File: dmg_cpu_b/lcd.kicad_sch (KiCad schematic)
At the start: 119 parts

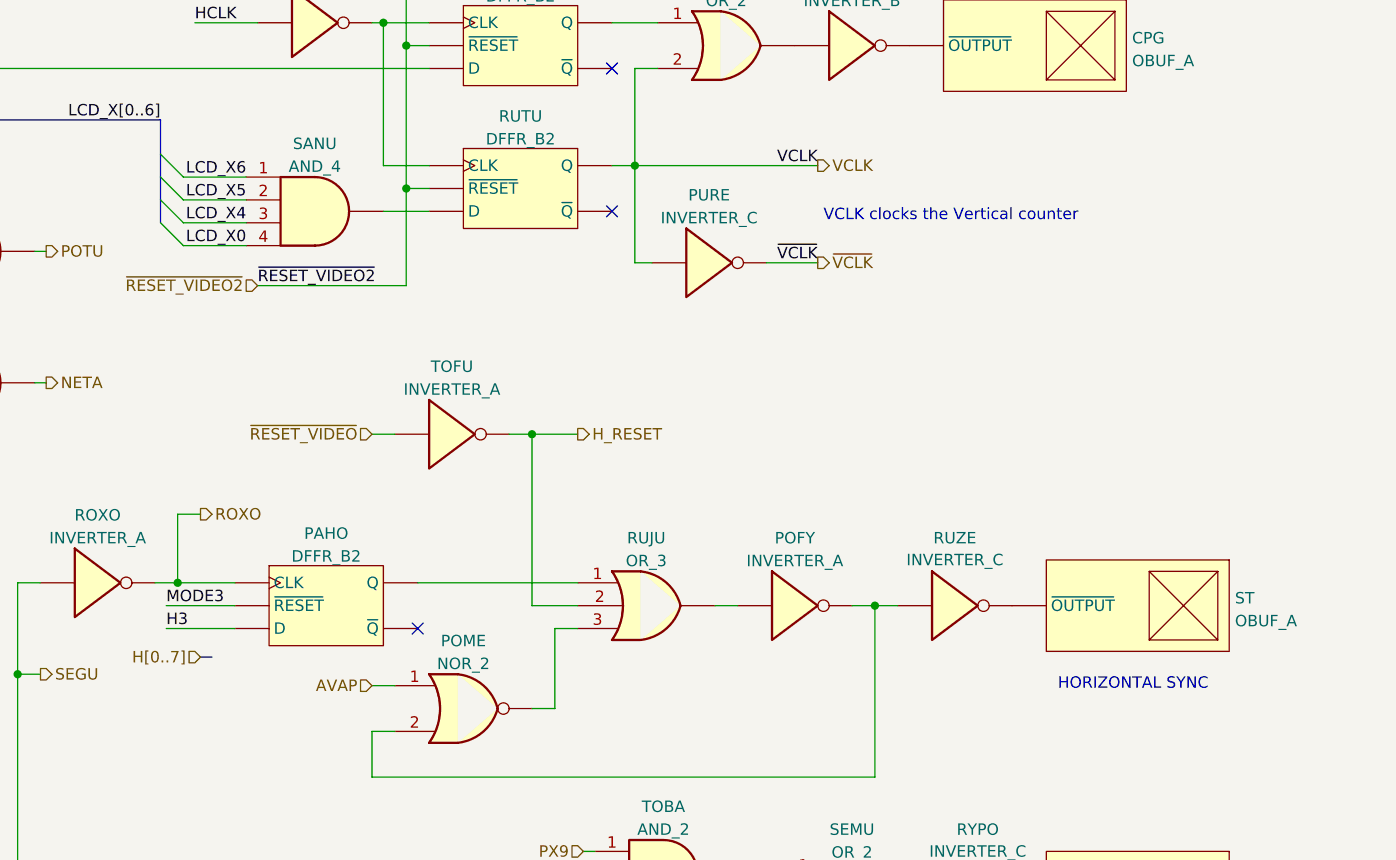
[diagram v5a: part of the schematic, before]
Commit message: more oam sheets added. Some are still work in progress.
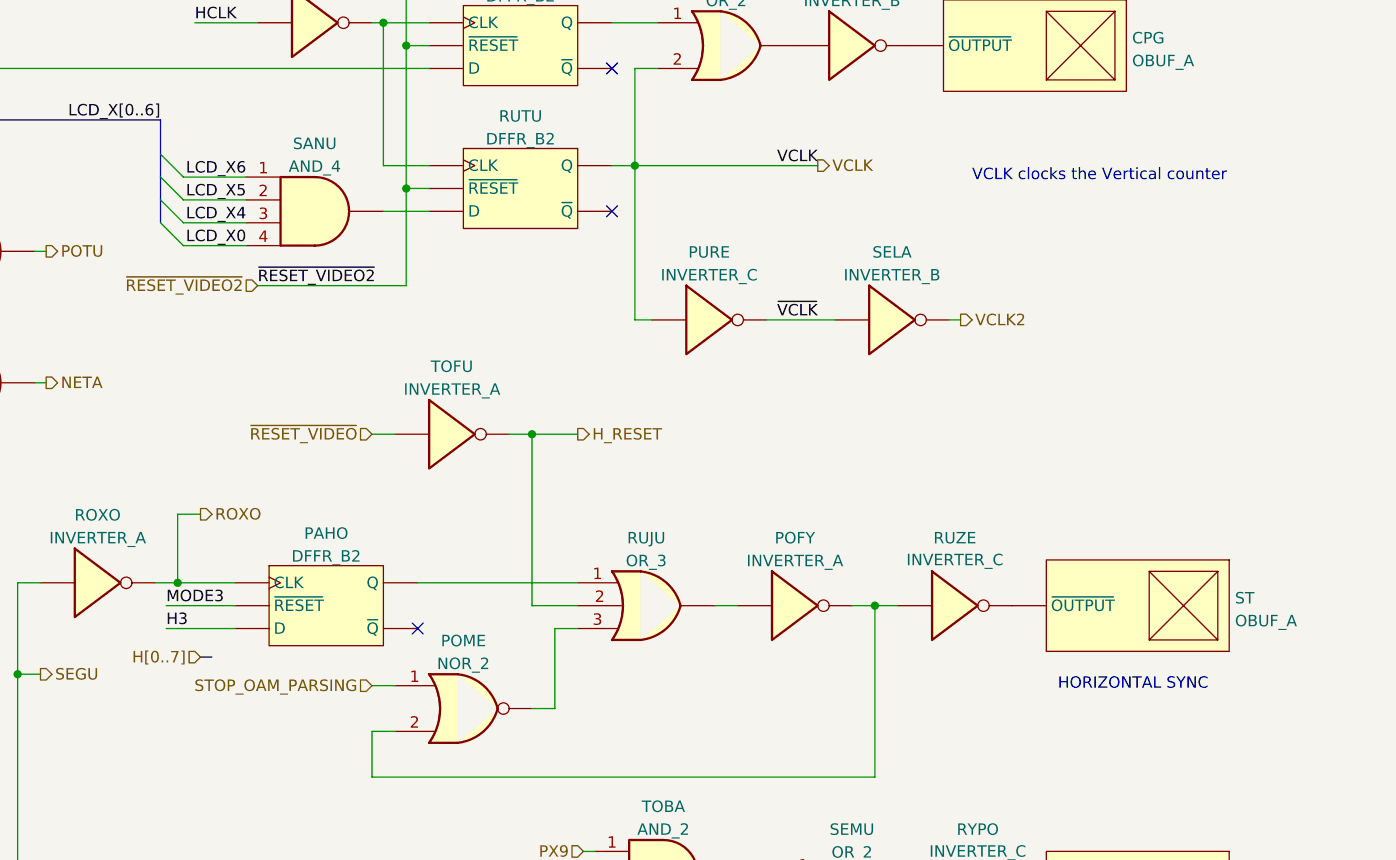
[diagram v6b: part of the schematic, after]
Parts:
- added SELA: INVERTER_B, symbol DMG_CPU_Cells:INVERTER_B
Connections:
- net ~{VCLK}: now also SELA.1
- net AVAP renamed STOP_OAM_PARSING
- new net VCLK2: SELA.2
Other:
- moved on the sheet: PURE
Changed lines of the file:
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@@
     (stroke (width 0) (type default) (color 0 0 0 0))
   )
-  (wire (pts (xy 327.025 173.99) (xy 325.12 173.99))
+  (wire (pts (xy 327.025 180.34) (xy 325.12 180.34))
     (stroke (width 0) (type default) (color 0 0 0 0))
   )
@@
     (stroke (width 0) (type default) (color 0 0 0 0))
   )
+  (wire (pts (xy 360.045 180.34) (xy 361.315 180.34))
+    (stroke (width 0) (type default) (color 0 0 0 0))
+  )
   (wire (pts (xy 322.58 163.195) (xy 325.12 163.195))
     (stroke (width 0) (type default) (color 0 0 0 0))
@@
     (stroke (width 0) (type default) (color 0 0 0 0))
   )
-  (wire (pts (xy 325.12 173.99) (xy 325.12 163.195))
+  (wire (pts (xy 325.12 180.34) (xy 325.12 163.195))
     (stroke (width 0) (type default) (color 0 0 0 0))
   )
@@
     (stroke (width 0) (type default) (color 0 0 0 0))
   )
-  (wire (pts (xy 339.725 173.99) (xy 345.44 173.99))
+  (wire (pts (xy 339.725 180.34) (xy 347.345 180.34))
     (stroke (width 0) (type default) (color 0 0 0 0))
   )
@@
     (effects (font (size 1.27 1.27)) (justify left bottom))
   )
-  (text "VCLK clocks the Vertical counter" (at 346.075 169.545 0)
+  (text "VCLK clocks the Vertical counter" (at 362.585 165.1 0)
     (effects (font (size 1.27 1.27)) (justify left bottom))
   )
@@
     (effects (font (size 1.27 1.27)) (justify left bottom))
   )
-  (label "~{VCLK}" (at 345.44 173.99 180)
+  (label "~{VCLK}" (at 345.44 180.34 180)
     (effects (font (size 1.27 1.27)) (justify right bottom))
   )
@@
     (effects (font (size 1.27 1.27)) (justify right))
   )
-  (hierarchical_label "AVAP" (shape input) (at 295.91 220.98 180)
+  (hierarchical_label "STOP_OAM_PARSING" (shape input) (at 295.91 220.98 180)
     (effects (font (size 1.27 1.27)) (justify right))
   )
@@
     (effects (font (size 1.27 1.27)) (justify left))
   )
+  (hierarchical_label "VCLK2" (shape output) (at 361.315 180.34 0)
+    (effects (font (size 1.27 1.27)) (justify left))
+  )
   (hierarchical_label "8192Hz" (shape input) (at 307.975 129.54 180)
     (effects (font (size 1.27 1.27)) (justify right))
   )
-  (hierarchical_label "~{VCLK}" (shape output) (at 345.44 173.99 0)
-    (effects (font (size 1.27 1.27)) (justify left))
-  )
   (hierarchical_label "FF40_D[0..7]" (shape input) (at 299.72 92.075 180)
     (effects (font (size 1.27 1.27)) (justify right))
@@
     (pin "2")
   )
-  (symbol (lib_id "DMG_CPU_Cells:INVERTER_C") (at 333.375 173.99 0) (unit 1)
+  (symbol (lib_id "DMG_CPU_Cells:INVERTER_C") (at 333.375 180.34 0) (unit 1)
     (in_bom yes) (on_board yes) (fields_autoplaced)
-    (property "Reference" "PURE" (id 0) (at 333.375 166.4802 0))
-    (property "Value" "INVERTER_C" (id 1) (at 333.375 169.0171 0))
-    (property "Footprint" "" (id 2) (at 330.835 173.99 0)
+    (property "Reference" "PURE" (id 0) (at 333.375 172.8302 0))
+    (property "Value" "INVERTER_C" (id 1) (at 333.375 175.3671 0))
+    (property "Footprint" "" (id 2) (at 330.835 180.34 0)
       (effects (font (size 1.27 1.27)) hide)
     )
-    (property "Datasheet" "http://iceboy.a-singer.de/doc/dmg_cells.html#inv_c" (id 3) (at 334.645 181.61 0)
+    (property "Datasheet" "http://iceboy.a-singer.de/doc/dmg_cells.html#inv_c" (id 3) (at 334.645 187.96 0)
       (effects (font (size 1.27 1.27)) hide)
     )
@@
     (pin "6")
   )
+  (symbol (lib_id "DMG_CPU_Cells:INVERTER_B") (at 353.695 180.34 0) (unit 1)
+    (in_bom yes) (on_board yes)
+    (property "Reference" "SELA" (id 0) (at 353.695 172.8302 0))
+    (property "Value" "INVERTER_B" (id 1) (at 353.695 175.3671 0))
+    (property "Footprint" "" (id 2) (at 351.155 180.34 0)
+      (effects (font (size 1.27 1.27)) hide)
+    )
+    (property "Datasheet" "http://iceboy.a-singer.de/doc/dmg_cells.html#inv_b" (id 3) (at 354.965 187.96 0)
+      (effects (font (size 1.27 1.27)) hide)
+    )
+    (pin "1")
+    (pin "2")
+  )
   (symbol (lib_id "DMG_CPU_Cells:DFFR_B2") (at 139.7 104.14 0) (unit 1)
